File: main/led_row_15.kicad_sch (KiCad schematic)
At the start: 30 parts

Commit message: Initial schematic complete
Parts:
- removed C96: 100nF, symbol Device:C_Small
- removed D168: SK6812MINI-E, bigbutton:LED_SK6812_MINI_E_REVERSE, symbol chonc60:SK6812MINI-E
- renumbered C82 to C501, C83 to C502, C84 to C503, C85 to C504, C86 to C505, C87 to C506, C88 to C507, C89 to C508, C90 to C509, C91 to C510, C92 to C511, C93 to C512, C94 to C513, C95 to C514, D154 to D501, D155 to D502, D156 to D503, D157 to D504, D158 to D505, D159 to D506, D160 to D507, D161 to D508, D162 to D509, D163 to D510, D164 to D511, D165 to D512, D166 to D513, D167 to D514
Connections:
- net LED_OUT: now also D514.2 (DOUT)

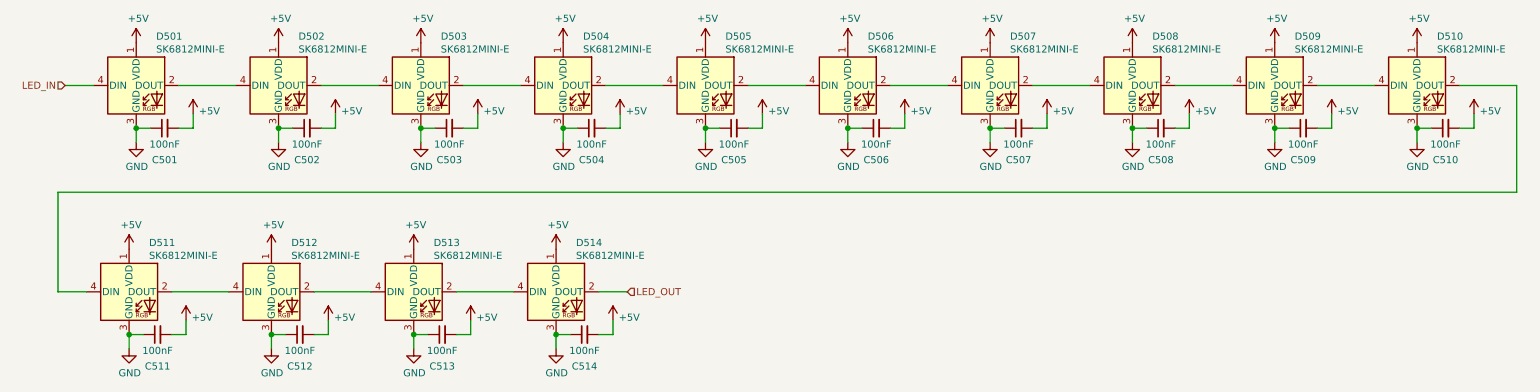
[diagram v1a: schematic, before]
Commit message: Start placing components
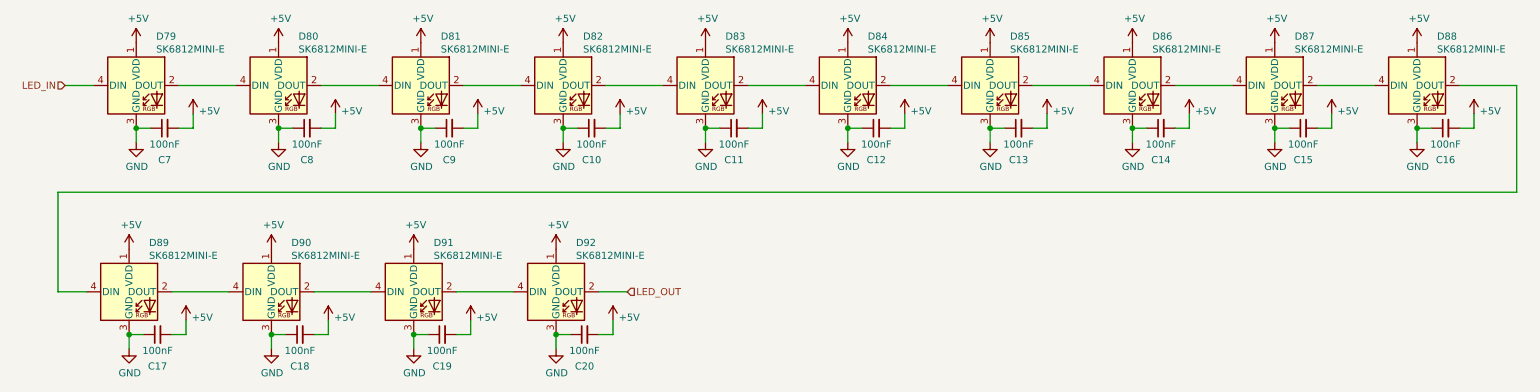
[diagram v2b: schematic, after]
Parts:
- C10: renamed from C504; footprint (none) -> Capacitor_SMD:C_0603_1608Metric
- C11: renamed from C505; footprint (none) -> Capacitor_SMD:C_0603_1608Metric
- C12: renamed from C506; footprint (none) -> Capacitor_SMD:C_0603_1608Metric
- C13: renamed from C507; footprint (none) -> Capacitor_SMD:C_0603_1608Metric
- C14: renamed from C508; footprint (none) -> Capacitor_SMD:C_0603_1608Metric
- C15: renamed from C509; footprint (none) -> Capacitor_SMD:C_0603_1608Metric
- C16: renamed from C510; footprint (none) -> Capacitor_SMD:C_0603_1608Metric
- C17: renamed from C511; footprint (none) -> Capacitor_SMD:C_0603_1608Metric
- C18: renamed from C512; footprint (none) -> Capacitor_SMD:C_0603_1608Metric
- C19: renamed from C513; footprint (none) -> Capacitor_SMD:C_0603_1608Metric
- C20: renamed from C514; footprint (none) -> Capacitor_SMD:C_0603_1608Metric
- C7: renamed from C501; footprint (none) -> Capacitor_SMD:C_0603_1608Metric
- C8: renamed from C502; footprint (none) -> Capacitor_SMD:C_0603_1608Metric
- C9: renamed from C503; footprint (none) -> Capacitor_SMD:C_0603_1608Metric
- D79: renamed from D501; footprint bigbutton:LED_SK6812_MINI_E_REVERSE -> chonc60:LED_SK6812_MINI_E_REVERSE
- D80: renamed from D502; footprint bigbutton:LED_SK6812_MINI_E_REVERSE -> chonc60:LED_SK6812_MINI_E_REVERSE
- D81: renamed from D503; footprint bigbutton:LED_SK6812_MINI_E_REVERSE -> chonc60:LED_SK6812_MINI_E_REVERSE
- D82: renamed from D504; footprint bigbutton:LED_SK6812_MINI_E_REVERSE -> chonc60:LED_SK6812_MINI_E_REVERSE
- D83: renamed from D505; footprint bigbutton:LED_SK6812_MINI_E_REVERSE -> chonc60:LED_SK6812_MINI_E_REVERSE
- D84: renamed from D506; footprint bigbutton:LED_SK6812_MINI_E_REVERSE -> chonc60:LED_SK6812_MINI_E_REVERSE
- D85: renamed from D507; footprint bigbutton:LED_SK6812_MINI_E_REVERSE -> chonc60:LED_SK6812_MINI_E_REVERSE
- D86: renamed from D508; footprint bigbutton:LED_SK6812_MINI_E_REVERSE -> chonc60:LED_SK6812_MINI_E_REVERSE
- D87: renamed from D509; footprint bigbutton:LED_SK6812_MINI_E_REVERSE -> chonc60:LED_SK6812_MINI_E_REVERSE
- D88: renamed from D510; footprint bigbutton:LED_SK6812_MINI_E_REVERSE -> chonc60:LED_SK6812_MINI_E_REVERSE
- D89: renamed from D511; footprint bigbutton:LED_SK6812_MINI_E_REVERSE -> chonc60:LED_SK6812_MINI_E_REVERSE
- D90: renamed from D512; footprint bigbutton:LED_SK6812_MINI_E_REVERSE -> chonc60:LED_SK6812_MINI_E_REVERSE
- D91: renamed from D513; footprint bigbutton:LED_SK6812_MINI_E_REVERSE -> chonc60:LED_SK6812_MINI_E_REVERSE
- D92: renamed from D514; footprint bigbutton:LED_SK6812_MINI_E_REVERSE -> chonc60:LED_SK6812_MINI_E_REVERSE

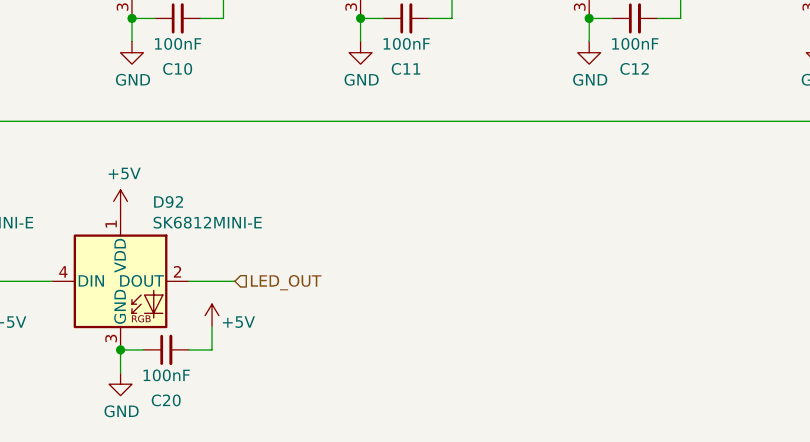
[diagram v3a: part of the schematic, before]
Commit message: Place LEDs, start routing
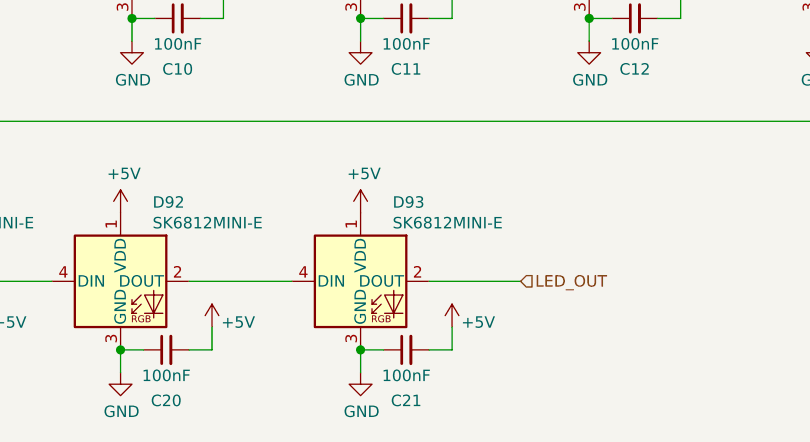
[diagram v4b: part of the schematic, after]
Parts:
- added C21: 100nF, Capacitor_SMD:C_0603_1608Metric, symbol Device:C_Small
- added D93: SK6812MINI-E, chonc60:LED_SK6812_MINI_E_REVERSE, symbol chonc60:SK6812MINI-E
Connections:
- net +5V: now also C21.2, D93.1 (VDD)
- net GND: now also C21.1, D93.3 (GND)
- net LED_OUT: now also D93.2 (DOUT); no longer D92.2 (DOUT)
- new net: D92.2 (DOUT), D93.4 (DIN)
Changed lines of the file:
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@@
   (junction (at 110.49 34.29) (diameter 1.016) (color 0 0 0 0))
   (junction (at 135.89 34.29) (diameter 1.016) (color 0 0 0 0))
+  (junction (at 135.89 71.12) (diameter 1.016) (color 0 0 0 0))
   (junction (at 161.29 34.29) (diameter 1.016) (color 0 0 0 0))
   (junction (at 186.69 34.29) (diameter 1.016) (color 0 0 0 0))
@@
     (stroke (width 0) (type solid) (color 0 0 0 0))
   )
-  (wire (pts (xy 116.84 63.5) (xy 121.92 63.5))
+  (wire (pts (xy 116.84 63.5) (xy 128.27 63.5))
     (stroke (width 0) (type solid) (color 0 0 0 0))
   )
@@
     (stroke (width 0) (type solid) (color 0 0 0 0))
   )
+  (wire (pts (xy 135.89 71.12) (xy 138.43 71.12))
+    (stroke (width 0) (type solid) (color 0 0 0 0))
+  )
+  (wire (pts (xy 135.89 73.66) (xy 135.89 71.12))
+    (stroke (width 0) (type solid) (color 0 0 0 0))
+  )
   (wire (pts (xy 143.51 26.67) (xy 153.67 26.67))
     (stroke (width 0) (type solid) (color 0 0 0 0))
@@
     (stroke (width 0) (type solid) (color 0 0 0 0))
   )
+  (wire (pts (xy 143.51 63.5) (xy 153.67 63.5))
+    (stroke (width 0) (type solid) (color 0 0 0 0))
+  )
+  (wire (pts (xy 143.51 71.12) (xy 146.05 71.12))
+    (stroke (width 0) (type solid) (color 0 0 0 0))
+  )
   (wire (pts (xy 146.05 31.75) (xy 146.05 34.29))
+    (stroke (width 0) (type solid) (color 0 0 0 0))
+  )
+  (wire (pts (xy 146.05 68.58) (xy 146.05 71.12))
     (stroke (width 0) (type solid) (color 0 0 0 0))
   )
@@
     (effects (font (size 1.27 1.27)) (justify right))
   )
-  (hierarchical_label "LED_OUT" (shape input) (at 121.92 63.5 0)
+  (hierarchical_label "LED_OUT" (shape input) (at 153.67 63.5 0)
     (effects (font (size 1.27 1.27)) (justify left))
   )
@@
     (pin "1")
   )
+  (symbol (lib_id "power:+5V") (at 135.89 55.88 0) (unit 1)
+    (in_bom yes) (on_board yes)
+    (property "Reference" "#PWR053" (id 0) (at 135.89 59.69 0)
+      (effects (font (size 1.27 1.27)) hide)
+    )
+    (property "Value" "+5V" (id 1) (at 136.2583 51.5556 0))
+    (property "Footprint" "" (id 2) (at 135.89 55.88 0)
+      (effects (font (size 1.27 1.27)) hide)
+    )
+    (property "Datasheet" "" (id 3) (at 135.89 55.88 0)
+      (effects (font (size 1.27 1.27)) hide)
+    )
+    (pin "1")
+  )
   (symbol (lib_id "power:+5V") (at 146.05 31.75 0) (unit 1)
     (in_bom yes) (on_board yes)
@@
     (pin "1")
   )
+  (symbol (lib_id "power:+5V") (at 146.05 68.58 0) (unit 1)
+    (in_bom yes) (on_board yes)
+    (property "Reference" "#PWR058" (id 0) (at 146.05 72.39 0)
+      (effects (font (size 1.27 1.27)) hide)
+    )
+    (property "Value" "+5V" (id 1) (at 148.9583 68.0656 0))
+    (property "Footprint" "" (id 2) (at 146.05 68.58 0)
+      (effects (font (size 1.27 1.27)) hide)
+    )
+    (property "Datasheet" "" (id 3) (at 146.05 68.58 0)
+      (effects (font (size 1.27 1.27)) hide)
+    )
+    (pin "1")
+  )
   (symbol (lib_id "power:+5V") (at 161.29 19.05 0) (unit 1)
     (in_bom yes) (on_board yes)
@@
     )
     (property "Datasheet" "" (id 3) (at 135.89 36.83 0)
+      (effects (font (size 1.27 1.27)) hide)
+    )
+    (pin "1")
+  )
+  (symbol (lib_id "power:GND") (at 135.89 73.66 0) (unit 1)
+    (in_bom yes) (on_board yes)
+    (property "Reference" "#PWR063" (id 0) (at 135.89 80.01 0)
+      (effects (font (size 1.27 1.27)) hide)
+    )
+    (property "Value" "GND" (id 1) (at 136.0043 77.9844 0))
+    (property "Footprint" "" (id 2) (at 135.89 73.66 0)
+      (effects (font (size 1.27 1.27)) hide)
+    )
+    (property "Datasheet" "" (id 3) (at 135.89 73.66 0)
       (effects (font (size 1.27 1.27)) hide)
     )
@@
     (pin "2")
   )
+  (symbol (lib_id "Device:C_Small") (at 140.97 71.12 90) (unit 1)
+    (in_bom yes) (on_board yes)
+    (property "Reference" "C21" (id 0) (at 140.97 76.7777 90))
+    (property "Value" "100nF" (id 1) (at 140.97 73.996 90))
+    (property "Footprint" "Capacitor_SMD:C_0603_1608Metric" (id 2) (at 140.97 71.12 0)
+      (effects (font (size 1.27 1.27)) hide)
+    )
+    (property "Datasheet" "~" (id 3) (at 140.97 71.12 0)
+      (effects (font (size 1.27 1.27)) hide)
+    )
+    (pin "1")
+    (pin "2")
+  )
   (symbol (lib_id "Device:C_Small") (at 166.37 34.29 90) (unit 1)
     (in_bom yes) (on_board yes)
@@
       (effects (font (size 0 0)) hide)
     )
+    (pin "1")
+    (pin "2")
+    (pin "3")
+    (pin "4")
+  )
+  (symbol (lib_name "chonc60:SK6812MINI-E_13") (lib_id "chonc60:SK6812MINI-E") (at 135.89 63.5 0) (unit 1)
+    (in_bom yes) (on_board yes)
+    (property "Reference" "D93" (id 0) (at 139.4461 54.7306 0)
+      (effects (font (size 1.27 1.27)) (justify left))
+    )
+    (property "Value" "SK6812MINI-E" (id 1) (at 139.4461 57.0293 0)
+      (effects (font (size 1.27 1.27)) (justify left))
+    )
+    (property "Footprint" "chonc60:LED_SK6812_MINI_E_REVERSE" (id 2) (at 137.16 71.12 0)
+      (effects (font (size 1.27 1.27)) (justify left top) hide)
+    )
+    (property "Datasheet" "https://ecksteinimg.de/Datasheet/LED/LED0011/SK6812MINI-E_REV02_EN.pdf" (id 3) (at 138.43 73.025 0)
+      (effects (font (size 1.27 1.27)) (justify left top) hide)
+    )
+    (property "License" "This symbol is based off of the SK6812 official KiCad symbol and is thus under its modified CC-BY-SA 4.0 license instead of MIT" (id 4) (at 135.839 82.906 0)
+      (effects (font (size 0 0)) hide)
+    )

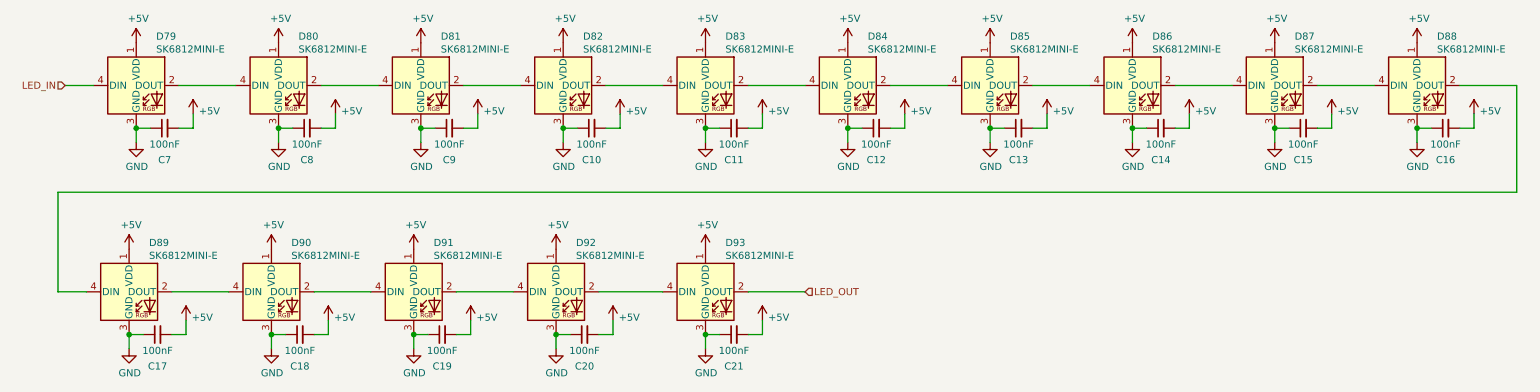
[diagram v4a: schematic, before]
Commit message: Update to new keyboard layout
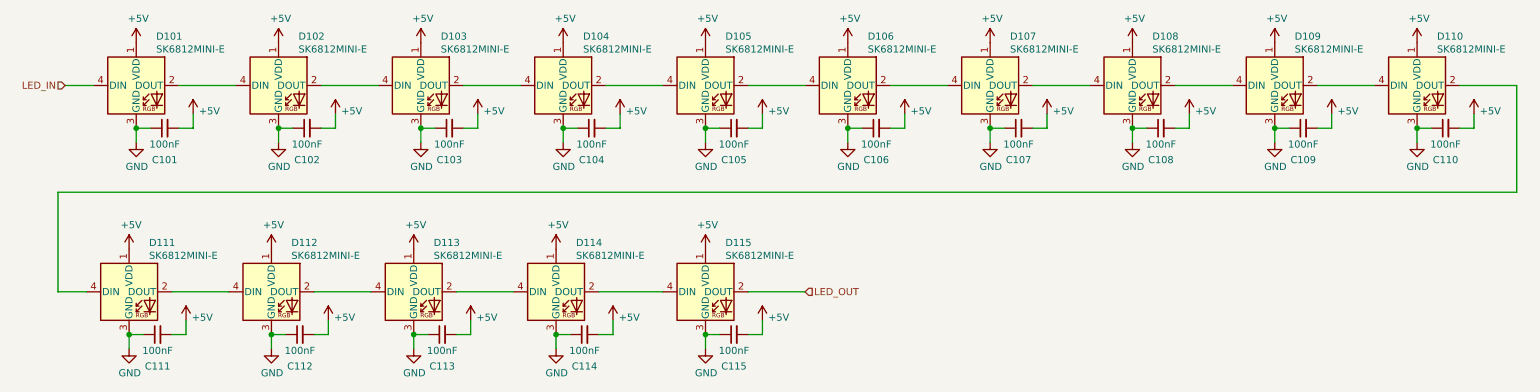
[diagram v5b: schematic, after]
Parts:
- renumbered C7 to C101, C8 to C102, C9 to C103, C10 to C104, C11 to C105, C12 to C106, C13 to C107, C14 to C108, C15 to C109, C16 to C110, C17 to C111, C18 to C112, C19 to C113, C20 to C114, C21 to C115, D79 to D101, D80 to D102, D81 to D103, D82 to D104, D83 to D105, D84 to D106, D85 to D107, D86 to D108, D87 to D109, D88 to D110, D89 to D111, D90 to D112, D91 to D113, D92 to D114, D93 to D115

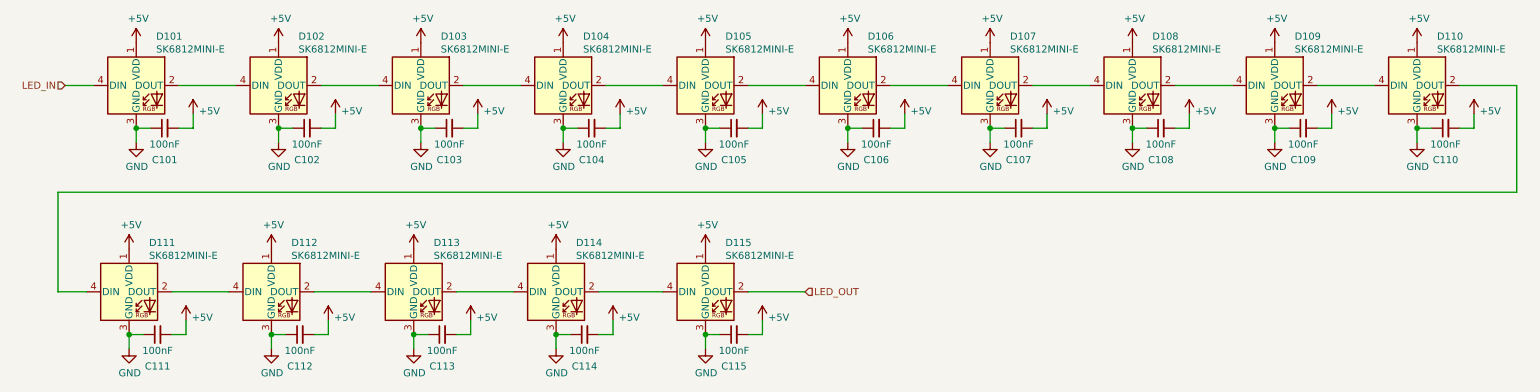
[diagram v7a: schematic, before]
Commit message: Switch to nRF58420 module and battery power
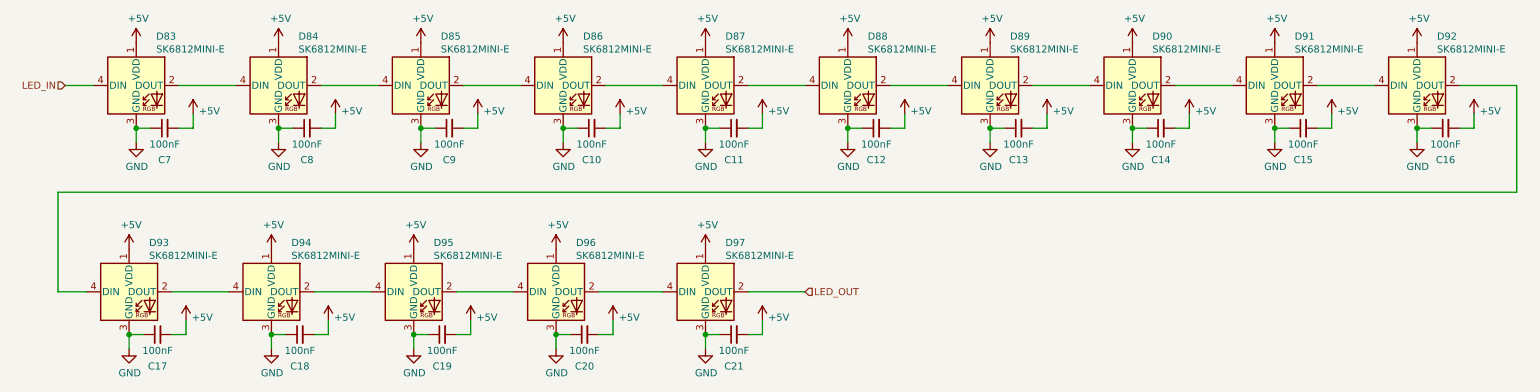
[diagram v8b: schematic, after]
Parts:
- renumbered C104 to C10, C105 to C11, C106 to C12, C107 to C13, C108 to C14, C109 to C15, C110 to C16, C111 to C17, C112 to C18, C113 to C19, C114 to C20, C115 to C21, C101 to C7, C102 to C8, C103 to C9, D101 to D83, D102 to D84, D103 to D85, D104 to D86, D105 to D87, D106 to D88, D107 to D89, D108 to D90, D109 to D91, D110 to D92, D111 to D93, D112 to D94, D113 to D95, D114 to D96, D115 to D97
